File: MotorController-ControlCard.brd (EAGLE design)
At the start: 160 x 100 mm, 46 parts, among them J1 SL07-HORIZ, J2 SL03THROUGH_HOLE, Q7 MOSFET-PCHANNEL, Q8 MOSFET-PCHANNEL, U2 MAX3232D, U4 TMS320F28069MPZT

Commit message: Finished Routing Board
Board is finished with routing, however it needs silkscreen to be done. Silk screen will be completed at a later date. There is one unbroken ground plain. Top plain is fairly broken as a ground plane, still considerred ground with via patching. Bottom is about the same as Top, but less broken. The Upper Middle is mostly unbroken and and the Lower Middle plain is unbroken.
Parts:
- moved R35 140.4 mm to (131.1, 88.1)
- moved R33 134.5 mm to (128.5, 88.1)
- moved R34 134.1 mm to (126.0, 88.1)
- moved Q8 125.2 mm to (131.1, 76.7), turned to 0 degrees
- moved C46 123.0 mm to (127.3, 71.6), turned to 270 degrees
- moved R11 107.3 mm to (102.9, 40.9), turned to 0 degrees
- moved C20 100.0 mm to (106.2, 45.2), turned to 270 degrees
- moved C22 97.3 mm to (110.0, 57.9), turned to 0 degrees
- moved C31 95.4 mm to (97.3, 74.4), turned to 270 degrees
- moved TP19 95.0 mm to (103.6, 45.2), turned to 270 degrees
- moved C28 95.0 mm to (104.9, 70.6), turned to 270 degrees
- moved C21 94.0 mm to (106.2, 60.5), turned to 0 degrees
- moved C29 93.0 mm to (101.1, 70.6), turned to 270 degrees
- moved C27 92.8 mm to (106.2, 59.2), turned to 0 degrees
- moved C25 92.2 mm to (106.2, 56.6), turned to 0 degrees
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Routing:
- net +3V3: track 0.00 -> 152.5 mm, vias 0 -> 1
- net VDDIO: track 0.00 -> 110.1 mm, vias 0 -> 6
- net NFAULT: track 0.00 -> 89.8 mm, vias 0 -> 2
- net NOCTW: track 0.00 -> 89.3 mm, vias 0 -> 2
- net TRST: track 0.00 -> 87.4 mm, vias 0 -> 1
- net VCC: track 0.00 -> 77.0 mm, vias 0 -> 2
- net TMS: track 0.00 -> 72.8 mm, vias 0 -> 1
- net TDO: track 0.00 -> 67.7 mm, vias 0 -> 1
- net TDI: track 0.00 -> 66.0 mm, vias 0 -> 1
- net UART_TX: track 0.00 -> 65.0 mm, vias 0 -> 1
- net UART_RX: track 0.00 -> 61.7 mm
- net TCK: track 0.00 -> 60.3 mm, vias 0 -> 1
- net PVDDSENSE: track 0.00 -> 58.4 mm, vias 0 -> 1
- net PWM_IN_NO_FILTER: track 0.00 -> 51.7 mm
- net BSENSE: track 0.00 -> 44.7 mm, vias 0 -> 1
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- added copper zone on layer 1, net GND
- added copper zone on layer 15, net GND
- added copper zone on layer 16, net GND
- added copper zone on layer 2, net GND
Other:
- board size 160 x 100 mm -> 73.9 x 65.7 mm

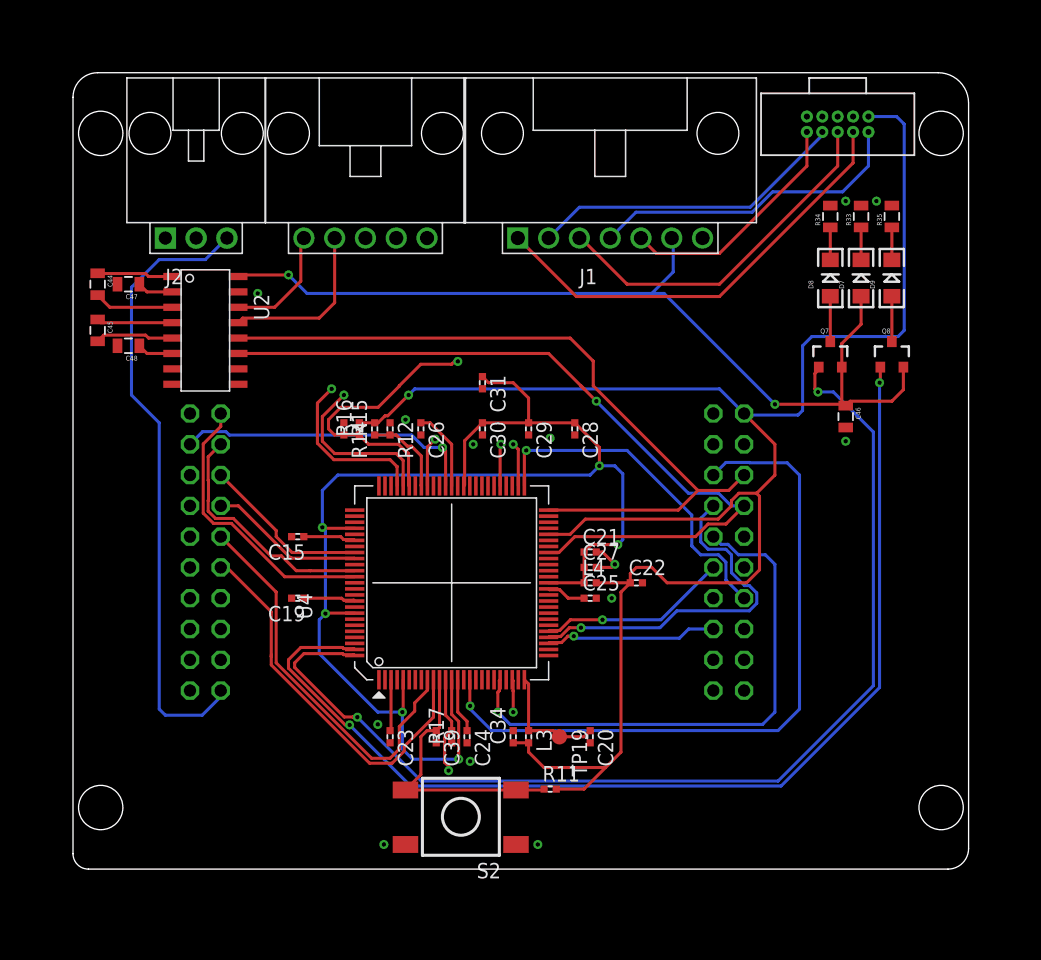
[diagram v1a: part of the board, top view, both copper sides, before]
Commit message: Rough Silkscreen Done
All items smashed and names and values put to sides of each component. some components names do not make sense or need clarification. Review with other members to be able determine extra silkscreen labeling needed for the board.
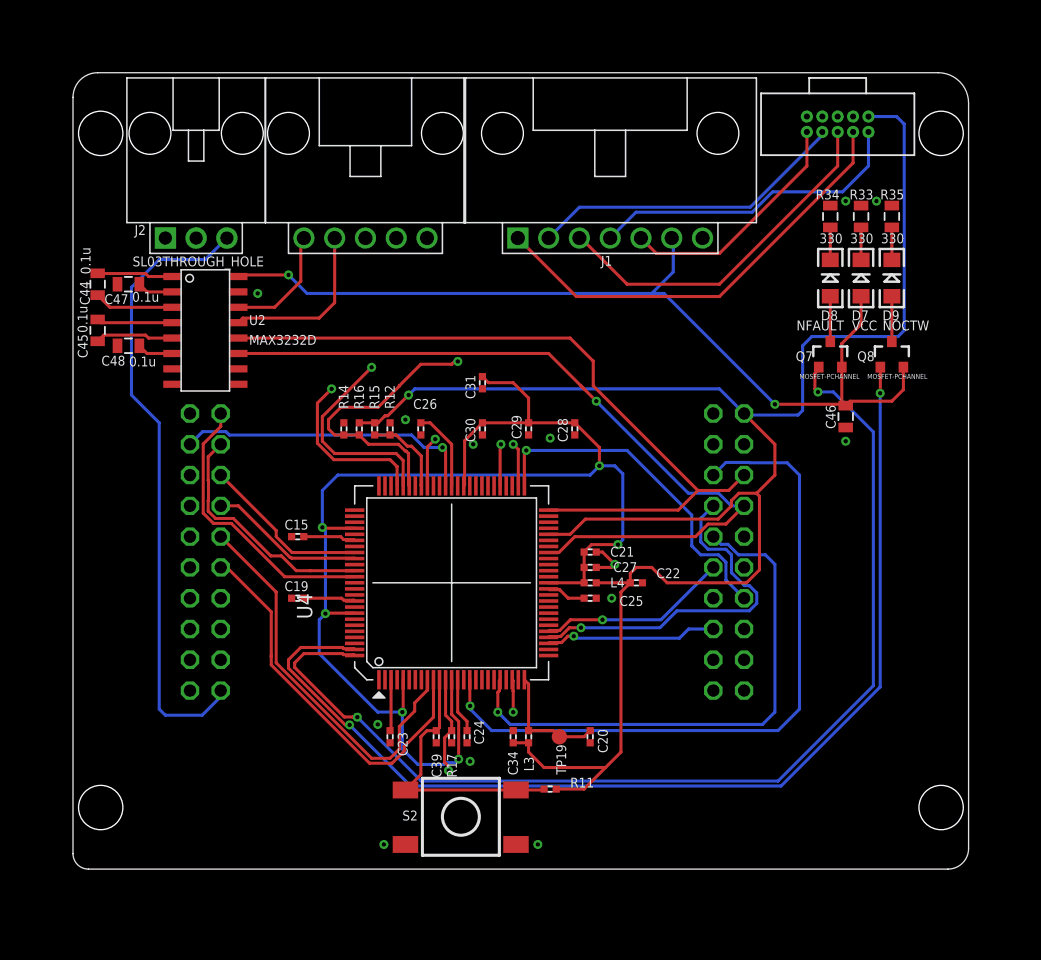
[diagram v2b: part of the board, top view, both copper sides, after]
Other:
- board outline removed
- board text added: "NFAULT"
- board text added: "NOCTW"
- board text added: "VCC"

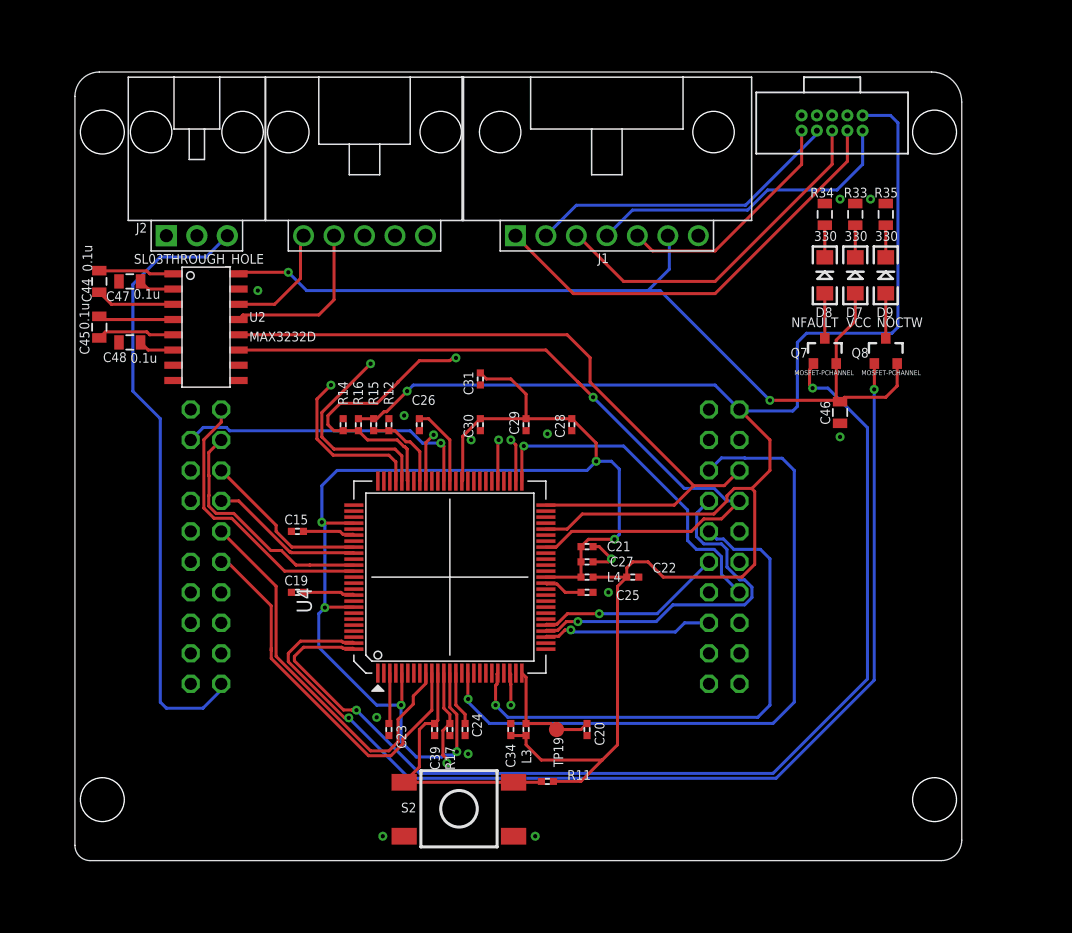
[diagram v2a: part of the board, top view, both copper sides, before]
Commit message: Updated silkscreen and moved reset switch
The board was shrunken for better fitting with boards that this card will be compatible with. Reset switch was moved to accomodate this. The Jtag connector routing was fixed due to a placement error. Silkscreen stating board and creators was added. Board should be ready for rev 1.
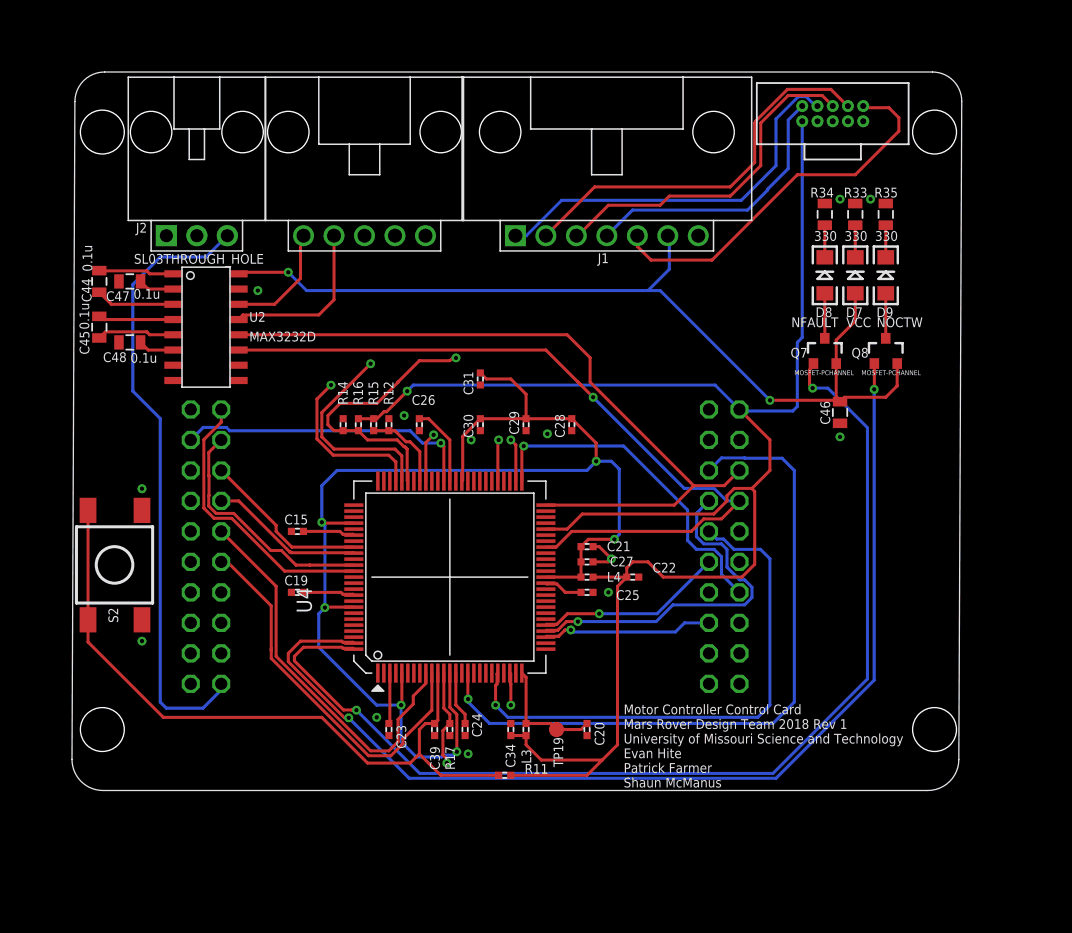
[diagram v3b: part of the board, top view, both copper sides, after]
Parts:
- moved S2 28.3 mm to (69.1, 54.4), turned to 180 degrees
- moved U$2 13.4 mm to (133.0, 94.0), turned to 90 degrees
- moved R11 3.59 mm to (99.3, 41.4)
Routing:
- net RESET#: track 22.2 -> 58.2 mm
- net TRST: track 87.4 -> 99.9 mm
- net +3V3: track 152.5 -> 145.3 mm
- net TDI: track 66.0 -> 72.4 mm
- net TCK: track 60.3 -> 56.1 mm
- net TMS: track 72.8 -> 69.3 mm
- net TDO: track 67.7 -> 66.6 mm
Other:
- board text added: "Motor Controller Control Card Mars Rover Design Team 2018 Rev 1 University of Missouri Science and Technology Evan Hite Patrick Farmer Shaun McManus"

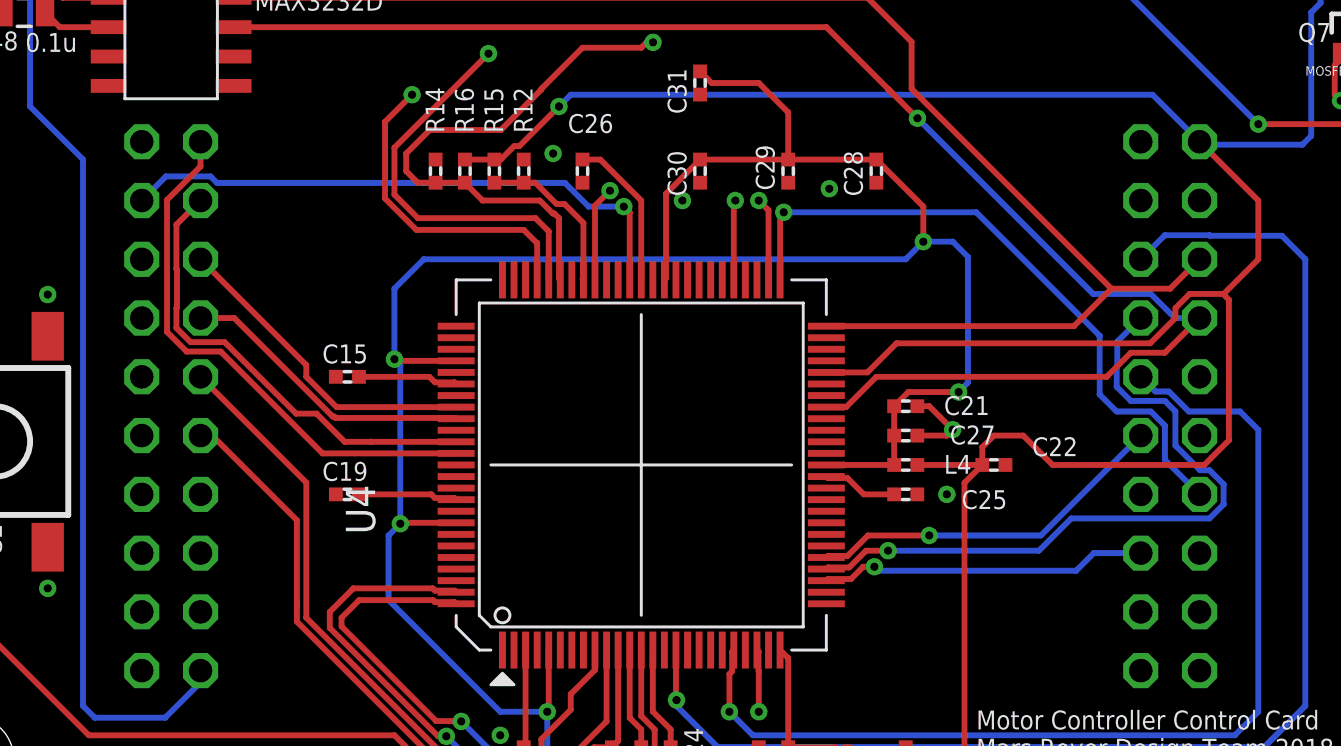
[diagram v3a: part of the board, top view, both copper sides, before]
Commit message: Adjusted net labeling, fixed schematic organization for clarity, fixed issues detected by ERC
Adjusted External Connections section components and labeling for clarity, resolved net connection issues on the microcontroller detected by ERC, added TDO flag to boot circuit for net connection clarity, removed redundant net labeling across schematic (previously contained both flags and on-line labels)
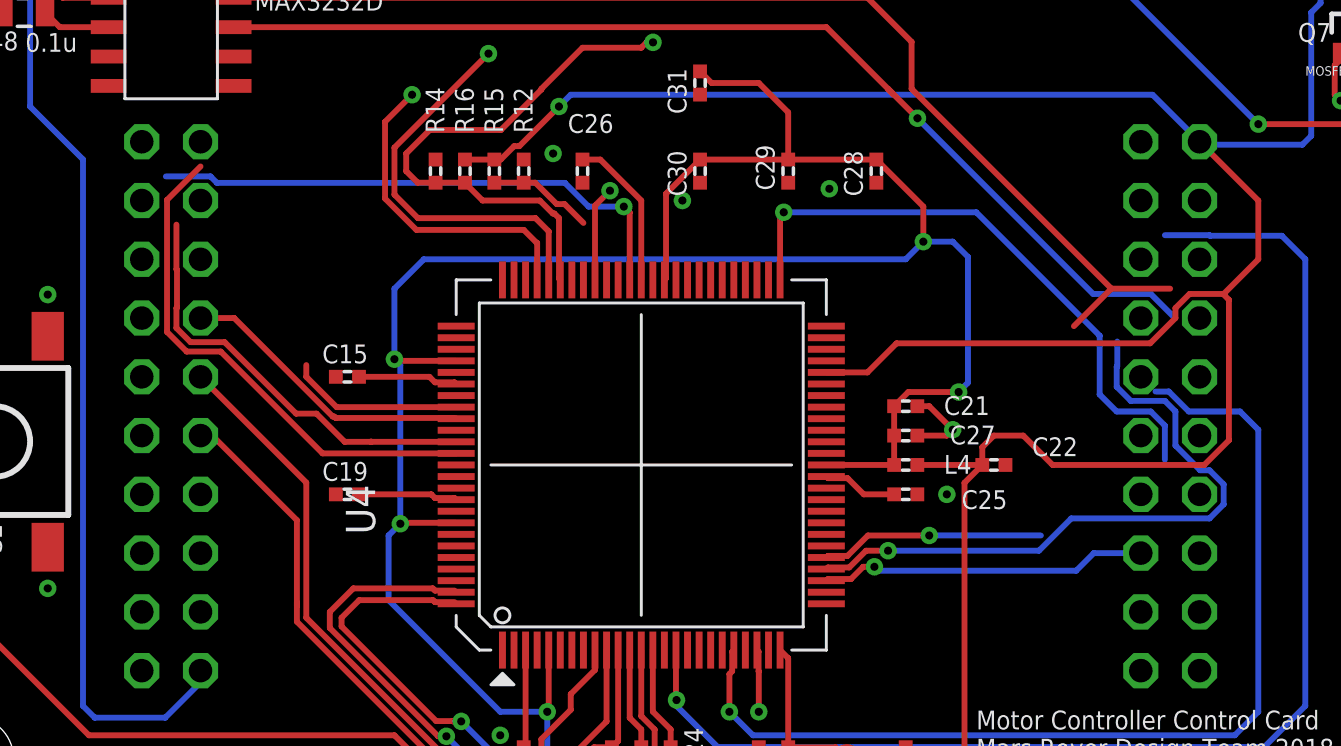
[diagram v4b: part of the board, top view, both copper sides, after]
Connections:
- removed net N$1: U$1.PA2
- removed net N$2: U$1.PA4
- removed net N$3: U$1.PA3
- removed net N$4: U$1.PA6
- removed net N$5: U$1.PA7
- removed net PWM_IN_NO_FILTER: J2.3, U$1.PF4
- net DC_CAL: now also U$1.PA3
- net EN_GATE: now also U$1.PA4
- net NFAULT: now also U$1.PA6
- net NOCTW: now also U$1.PA7
- net PWM_IN: now also J2.3, U$1.PF4, U4.49; no longer U4.75
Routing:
- net PWM_IN_NO_FILTER: track 51.7 -> 0.00 mm
- net PWM_IN: track 0.00 -> 51.7 mm
- net SDO: track 39.5 -> 0.00 mm, vias 1 -> 0
- net SDI: track 33.7 -> 0.00 mm, vias 1 -> 0
- net UART_TX: track 65.0 -> 46.2 mm
- net UART_RX: track 61.7 -> 49.2 mm
- net INL_B: track 14.0 -> 7.53 mm
- net CSENSE: track 15.8 -> 9.67 mm
- net GPIO34: track 7.09 -> 4.57 mm
- net SCLK: track 28.4 -> 26.2 mm
- net PVDDSENSE: track 58.4 -> 56.9 mm
- net NSCS: track 25.1 -> 23.6 mm
- net INL_A: track 20.1 -> 18.6 mm
- net ASENSE: track 29.8 -> 28.4 mm
- net INH_A: track 23.5 -> 22.4 mm
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
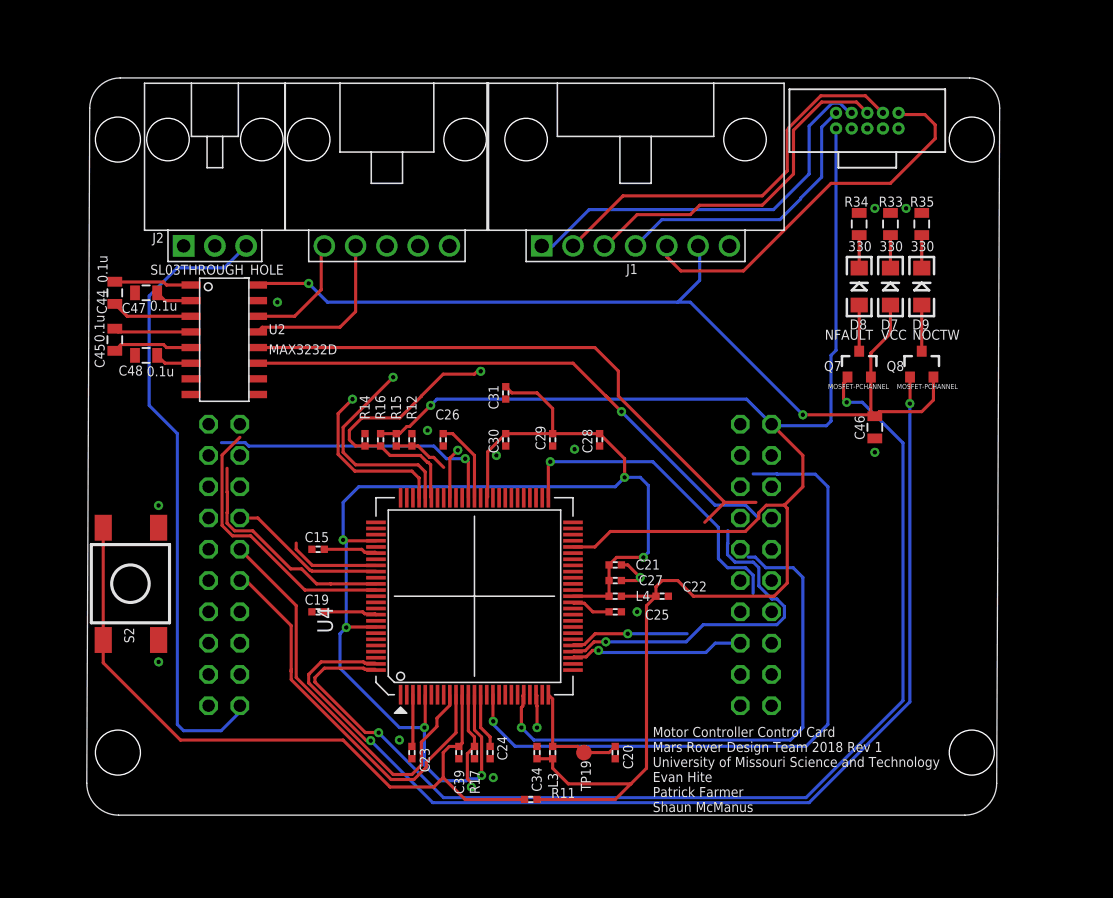
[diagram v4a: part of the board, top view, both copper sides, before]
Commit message: Routing and Silkscreen Update
New routes were made and Silkscreen changes were made. SL connectors are now labelled and arrows indicate direction of headers.
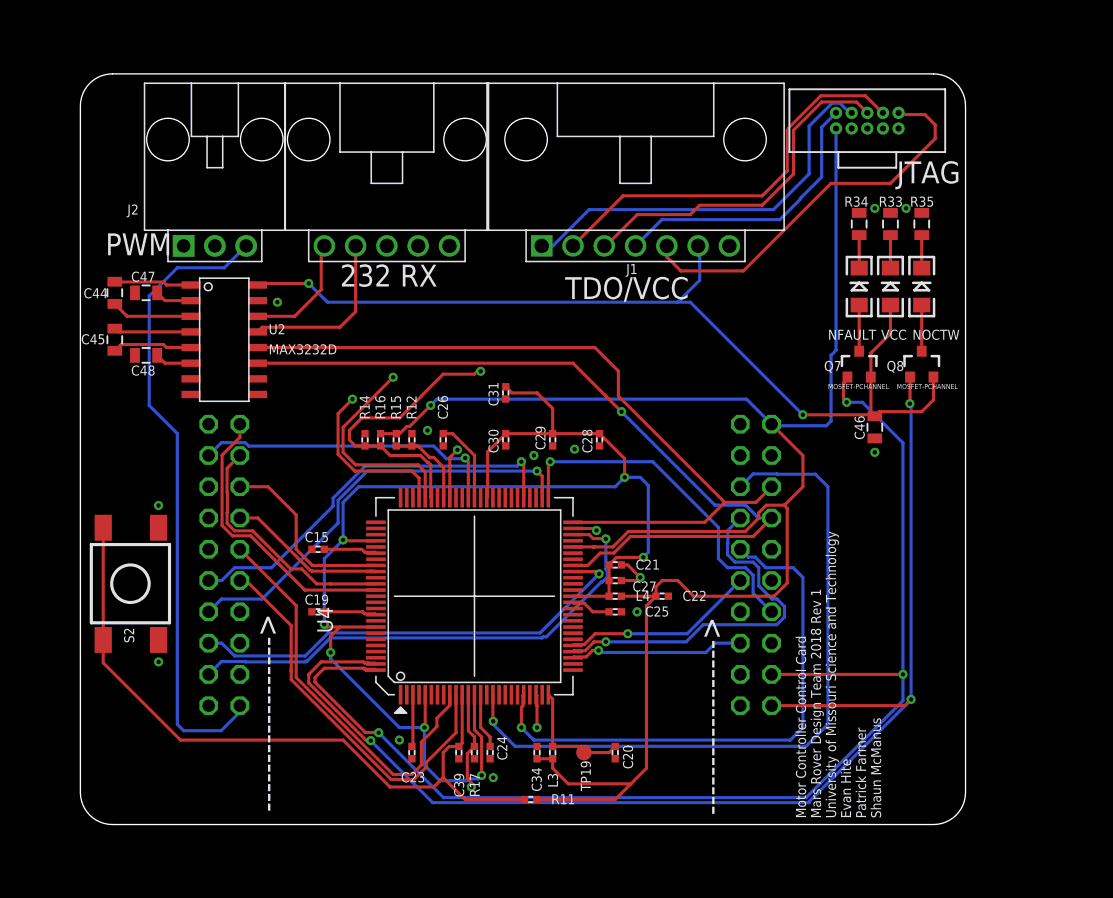
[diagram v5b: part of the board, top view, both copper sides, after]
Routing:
- net DC_CAL: track 0.00 -> 41.6 mm, vias 0 -> 1
- net EN_GATE: track 0.00 -> 37.1 mm, vias 0 -> 1
- net PWM_IN: track 51.7 -> 88.6 mm, vias 0 -> 1
- net SDO: track 0.00 -> 34.8 mm, vias 0 -> 1
- net SDI: track 0.00 -> 32.8 mm, vias 0 -> 1
- net UART_TX: track 46.2 -> 64.7 mm
- net UART_RX: track 49.2 -> 61.7 mm
- net NOCTW: track 89.2 -> 101.4 mm, vias 2 -> 3
- net NFAULT: track 89.7 -> 101.3 mm, vias 2 -> 3
- net INL_B: track 7.53 -> 15.3 mm
- net CSENSE: track 9.67 -> 15.8 mm
- net VDDIO: track 110.5 -> 113.1 mm, vias 6 -> 7
- net GPIO34: track 4.57 -> 7.03 mm
- net SCLK: track 26.2 -> 28.4 mm
- net NSCS: track 23.6 -> 25.2 mm
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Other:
- board outline added: 71.9 x 61 mm
- board text added: "------------------>"
- board text added: "232 RX"
- board text added: "JTAG"
- board text added: "PWM"
- board text added: "TDO/VCC"
